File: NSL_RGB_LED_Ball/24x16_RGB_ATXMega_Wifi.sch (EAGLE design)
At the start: 109 parts, among them IC2 TLC5947XLP, IC3 TLC5947XLP, IC4 TLC5947XLP, IC5 MCP73123, IC6 BLUETOOTH-RN41", IC7 MMA7455L, IC8 OPA344, Q1 BSH201, X1 NX3225GA XC1972CT-ND

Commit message: 
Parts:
- removed LED: (no value), led:LEDCHIP-LED0603
- removed R16: 2.2k, SparkFun:RESISTOR
- removed R17, R18, R19: 10k, SparkFun:RESISTOR
- removed R20: 1M, SparkFun:RESISTOR
- removed SJ3, SJ4: SOLDERJUMPERNO, SparkFun:SOLDERJUMPERNO
- removed U$5: ZG2100MC, zg2100-mrf24wb0ma:ZG2100MC
- added ANT: ANTENNA2SMD2, SparkFun:ANTENNA2SMD2
- added C23: .1uF, SparkFun:CAP0805
- added C24: 12pF, SparkFun:CAP0805
- added L1: NL, SparkFun:INDUCTOR0402
- added L2: 2.2nH, SparkFun:INDUCTOR0402
- C17: value .1uF -> 2.2pF; device SparkFun:CAP0805 -> SparkFun:CAP0402-CAP; MPN 08055C105MAT2A -> (none); OC_NEWARK 73T5385 -> (none)
- C18: value 0.1uF -> 10pF; device SparkFun:CAP0805 -> SparkFun:CAP0402-CAP; MPN 08055C104K4T2A -> (none); OC_NEWARK 95W2729 -> (none)
- C19: value 4.7uF -> 1uF; MPN 08053D475KAT2A -> (none); OC_NEWARK 15P4053 -> (none)
- C20: value 1uF -> 0.1uF; MPN 08055D105KAT2A -> 08055C104K4T2A; OC_NEWARK 66M3779 -> 95W2729
- C21: value .1uF -> 4.7uF; MPN 08055C105MAT2A -> 08053D475KAT2A; OC_NEWARK 73T5385 -> 15P4053
- C22: value 12pF -> 1uF; MF AVX CORPORATION -> (none); MPN 08055A120JAT2A -> 08055D105KAT2A; OC_NEWARK 30H0781 -> 66M3779
- IC6: value BLUETOOTH-RN41" -> CC3000; device NSL_Mini_Quad:BLUETOOTH-RN41" -> centerblack_engineering:CC3000; OC_NEWARK unknown -> (none)
- JP2: value USBSMD -> (none); device SparkFun-Connectors:USBSMD -> SparkFun-Connectors:M041.27MM
- JP3: value (none) -> USBSMD; device SparkFun-Connectors:M041.27MM -> SparkFun-Connectors:USBSMD
- R10: value 1k -> 4.7k; MF VISHAY/DALE -> (none); MPN CRCW08051K00FKTA -> CRCW08054K70FKEA; OC_NEWARK 05F1507 -> 61M5491
- R11: value 1k -> 2.2k; MF VISHAY/DALE -> (none); MPN CRCW08051K00FKTA -> CRCW08052K20FKEA; OC_NEWARK 05F1507 -> 61M5457
- R12, R13: value 1k -> 10k; MF VISHAY/DALE -> (none); MPN CRCW08051K00FKTA -> (none); OC_NEWARK 05F1507 -> unknown
- R14: value 220 -> 10k
- R15: value 4.7k -> 1M; MPN CRCW08054K70FKEA -> (none); OC_NEWARK 61M5491 -> unknown
- SJ1, SJ2: OC_NEWARK unknown -> (none)
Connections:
- removed net N$21: R12.1, SJ3.2
- removed net N$23: R11.1, SJ2.2
- removed net N$24: R13.1, SJ4.2
- removed net N$4: LED.C, R14.2
- removed net N$5: R10.1, SJ1.2
- removed net PIO3: IC6.PIO3, SJ3.1
- removed net PIO4: IC6.PIO4, SJ4.1
- removed net PIO5: IC6.PIO5, R14.1
- removed net PIO6: IC6.PIO6, SJ2.1
- removed net PIO7: IC6.PIO7, SJ1.1
- removed net RX: IC1.PC6/MISO/RXD1, IC6.UARTTX
- removed net TX: IC1.PC7/SCK/TXD1/CLKO/EVO, IC6.UARTRX
- new net MISO: IC1.PC6/MISO/RXD1, IC6.SPI_DOUT
- new net MOSI: IC1.PC5/OC1B/MOSI/XCK1, IC6.SPI_DIN
- new net N$22: C17.2, C18.1, L2.2
- new net N$25: ANT.SIGNAL, C17.1, L1.2
- new net N$26: IC6.SCL_CC3000, SJ1.1
- new net N$27: IC6.SCL_EEPROM, SJ1.2
- new net N$28: IC6.SDA_CC3000, SJ2.2
- new net N$29: IC6.SDA_EEPROM, SJ2.1
- new net N$8: C18.2, IC6.RF_ANT
- new net SCK: IC1.PC7/SCK/TXD1/CLKO/EVO, IC6.SPI_CLK
- new net SPI_IRQ: IC1.PC2/OC0C/RXD0, IC6.SPI_IRQ
- new net SS: IC1.PC4/OC1A/#SS, IC6.SPI_CS
- new net VBAT_SW_EN: IC1.PC1/OC0B/XCK0/SCL, IC6.VBAT_SW_EN
- new net VIO: IC1.PC0/OC0A/SDA, IC6.VIO_HOST
- new net WL_EN1: IC1.PB3/ADC11/DAC1, IC6.WL_EN1
- new net WL_EN2: IC1.PB2/ADC10/DAC0, IC6.WL_EN2
- net BT_RST: no longer IC6.RESET
- net D+: now also JP2.2, JP3.D+; no longer JP2.D+, JP3.2
- net D-: now also JP2.3, JP3.D-; no longer JP2.D-, JP3.3
- net GND: now also C19.1, C22.1, C23.2, IC6.EXT_32K, IC6.GND@10, IC6.GND@11, IC6.GND@16, IC6.GND@18, IC6.GND@20, IC6.GND@22, IC6.GND@25, IC6.GND@31, IC6.GND@32, IC6.GND@33, IC6.GND@34, IC6.GND@36, IC6.GND@37, IC6.GND@38, IC6.GND@39, IC6.GND@40, IC6.GND@41, IC6.GND@42, IC6.GND@43, IC6.GND@44, IC6.GND@45, IC6.GND@46, IC6.GND@9, JP2.4, JP3.GND, L1.1, L2.1, R10.1, R14.2; no longer C17.2, C18.1, C21.2, IC6.GND1, IC6.GND2, IC6.GND3, IC6.GND4, IC6.GND5, JP2.GND, JP3.4, R15.1, R19.2
- net MIC: now also C24.1, R15.2; no longer C22.1, R20.2
- net N$14: now also C21.2, R12.2; no longer C19.2, R17.2
- net N$15: now also C21.1, R11.1; no longer C19.1, R16.1
- net N$16: now also C22.2, R13.1, R14.1; no longer C20.2, R18.1, R19.1
- net N$17: now also C23.1, C24.2, R12.1, R15.1; no longer C21.1, C22.2, R17.1, R20.1
- net N$20: now also R10.2; no longer R15.2
- net N$7: now also JP2.1, JP3.VBUS; no longer JP2.VBUS, JP3.1
- net VCC: now also C20.2, R11.2, R13.2; no longer C18.2, R16.2, R18.2
- net VDD: now also C19.2, IC6.VBAT_IN; no longer C17.1, IC6.VDD, LED.A, R10.2, R11.2, R12.2, R13.2
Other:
- note added: "WiFi CC3000"
- note removed: "Bluetooth"

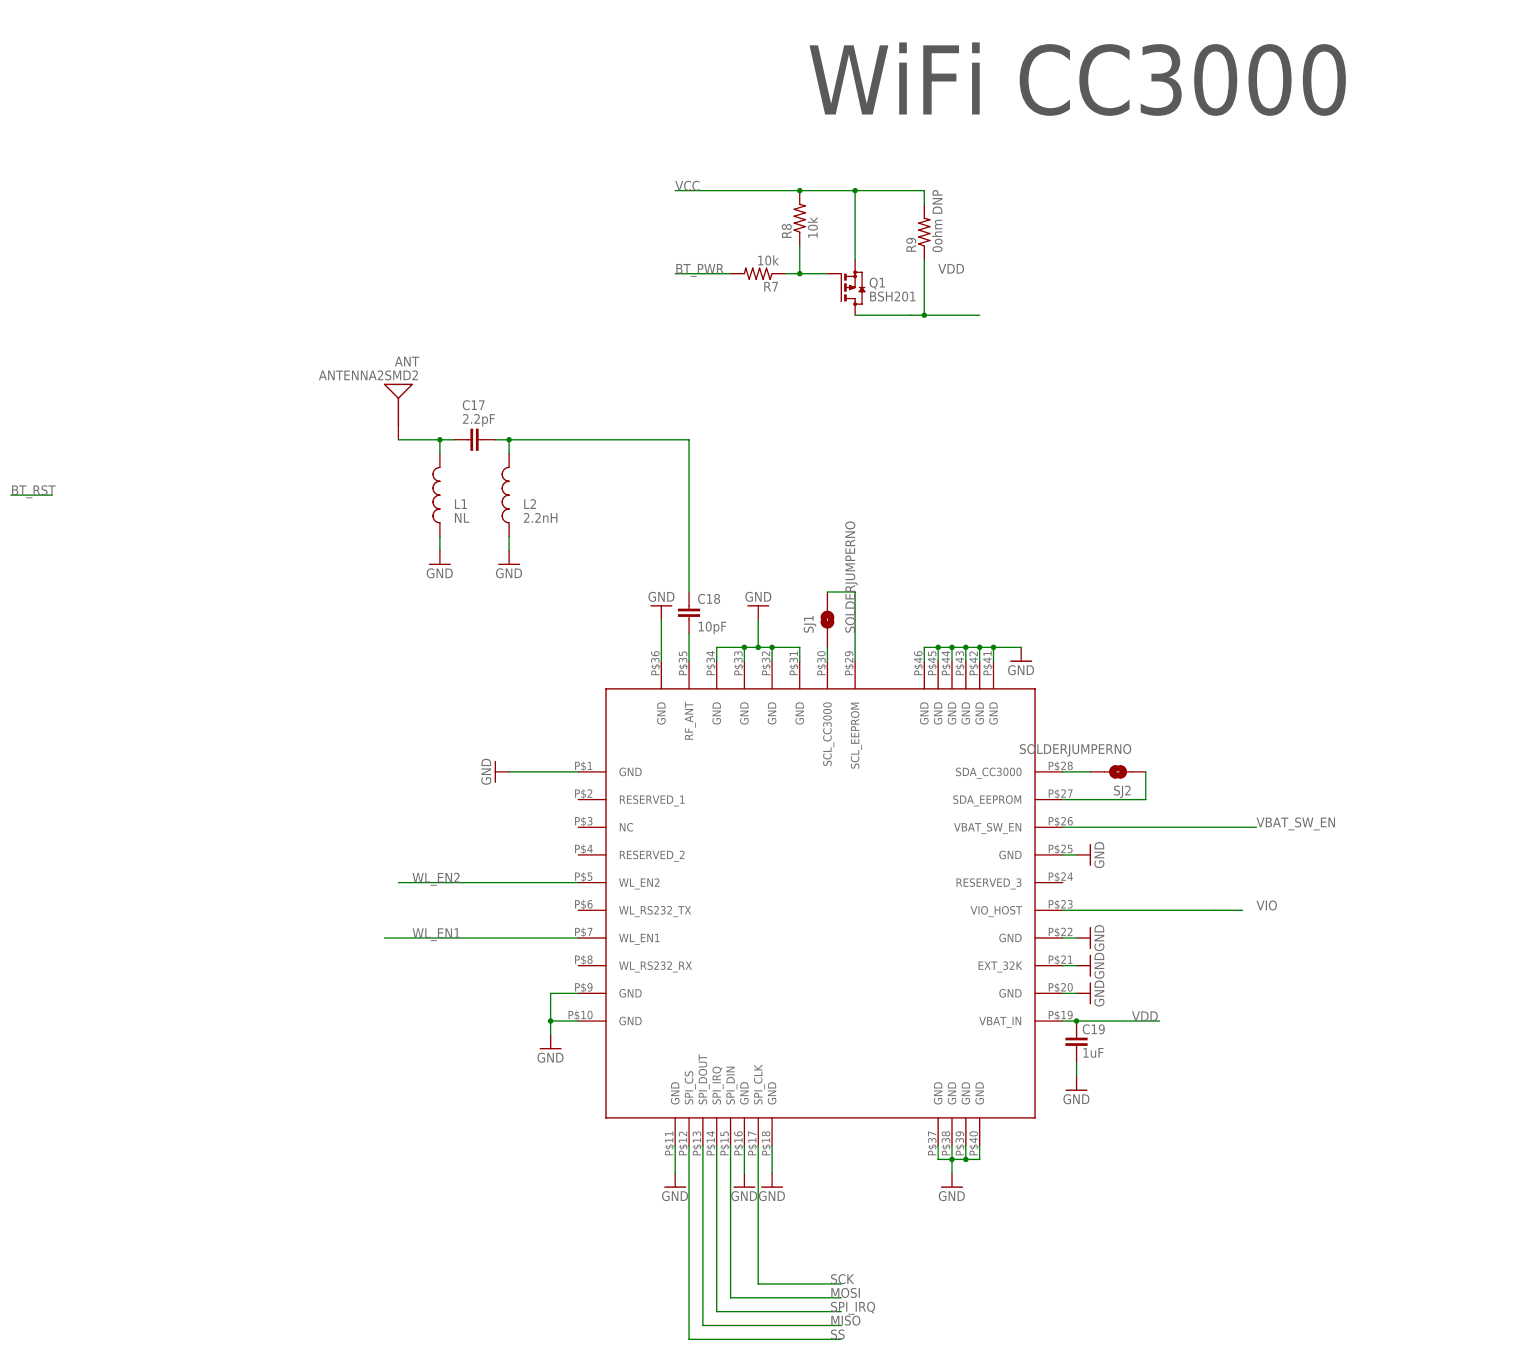
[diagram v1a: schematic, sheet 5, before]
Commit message: 
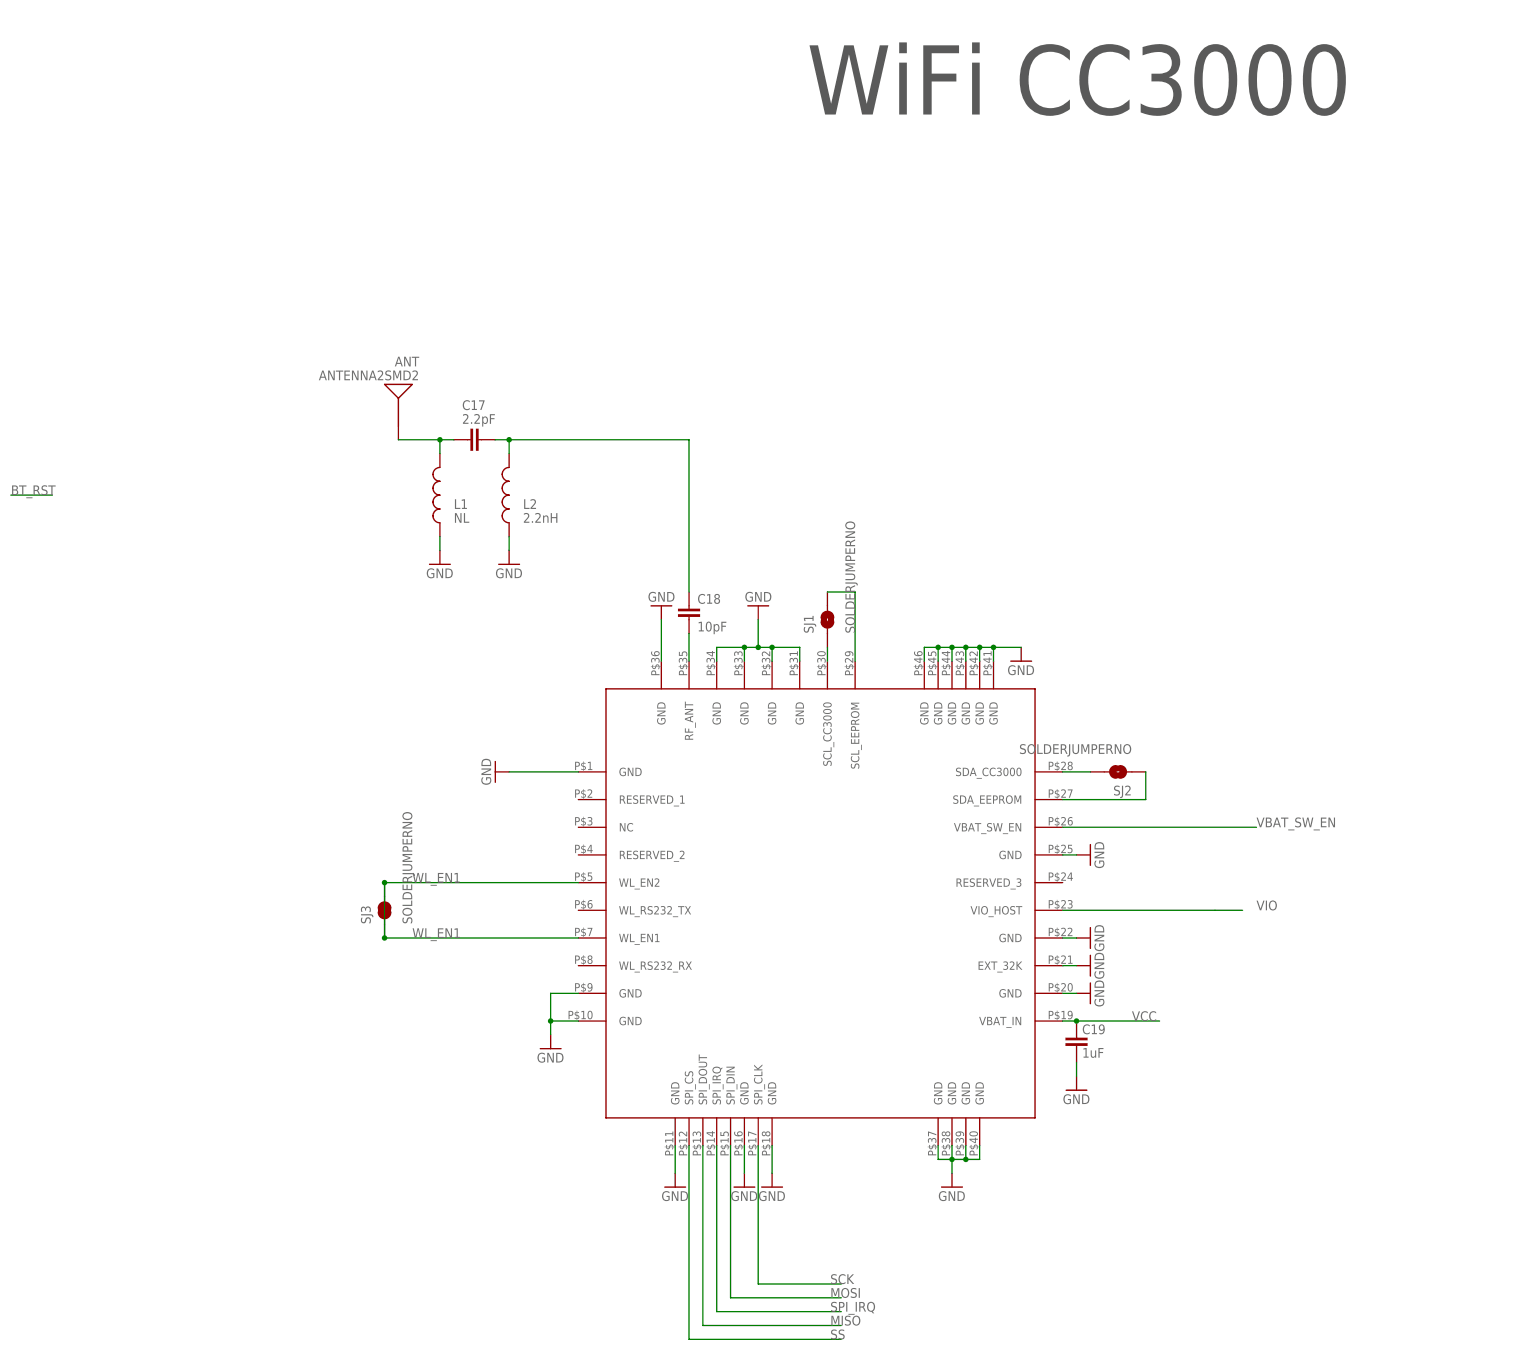
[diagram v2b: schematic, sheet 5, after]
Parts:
- removed Q1: BSH201, transistor-small-signal:BSS84
- removed R7, R8: 10k, SparkFun:RESISTOR
- removed R9: 0ohm DNP, SparkFun:RESISTOR
- added SJ3: SOLDERJUMPERNO, SparkFun:SOLDERJUMPERNO
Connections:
- removed net BT_PWR: IC1.PB1/ADC9, R7.2
- removed net N$18: Q1.G, R7.1, R8.1
- removed net VDD: C19.2, IC6.VBAT_IN, Q1.D, R9.1
- removed net WL_EN2: IC1.PB2/ADC10/DAC0, IC6.WL_EN2
- net VCC: now also C19.2, IC6.VBAT_IN; no longer Q1.S, R8.2, R9.2
- net WL_EN1: now also IC6.WL_EN2, SJ3.1, SJ3.2; no longer IC1.PB3/ADC11/DAC1
